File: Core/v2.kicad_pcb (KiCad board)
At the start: 4 copper layers, 80 x 43 mm, 120 parts, among them J1 JST_PH_S4B-PH-K, J2 JST_PH_S4B-PH-K, J3 JST_PH_S3B-PH-K, J4 JST_PH_S6B-PH-K, J5 JST_PH_S6B-PH-K, J6 Conn_02x06_Odd_Even, J7 Conn_01x02_Male, J8 Conn_01x02_Male, J9 Conn_02x06_Odd_Even, Q1 STD2805, U1 ADAU1452, U2 24AA1024, U3 AD1974, U4 AD1955, U5 AD1955, Y1 12.288MHz, Y2 12.288MHz

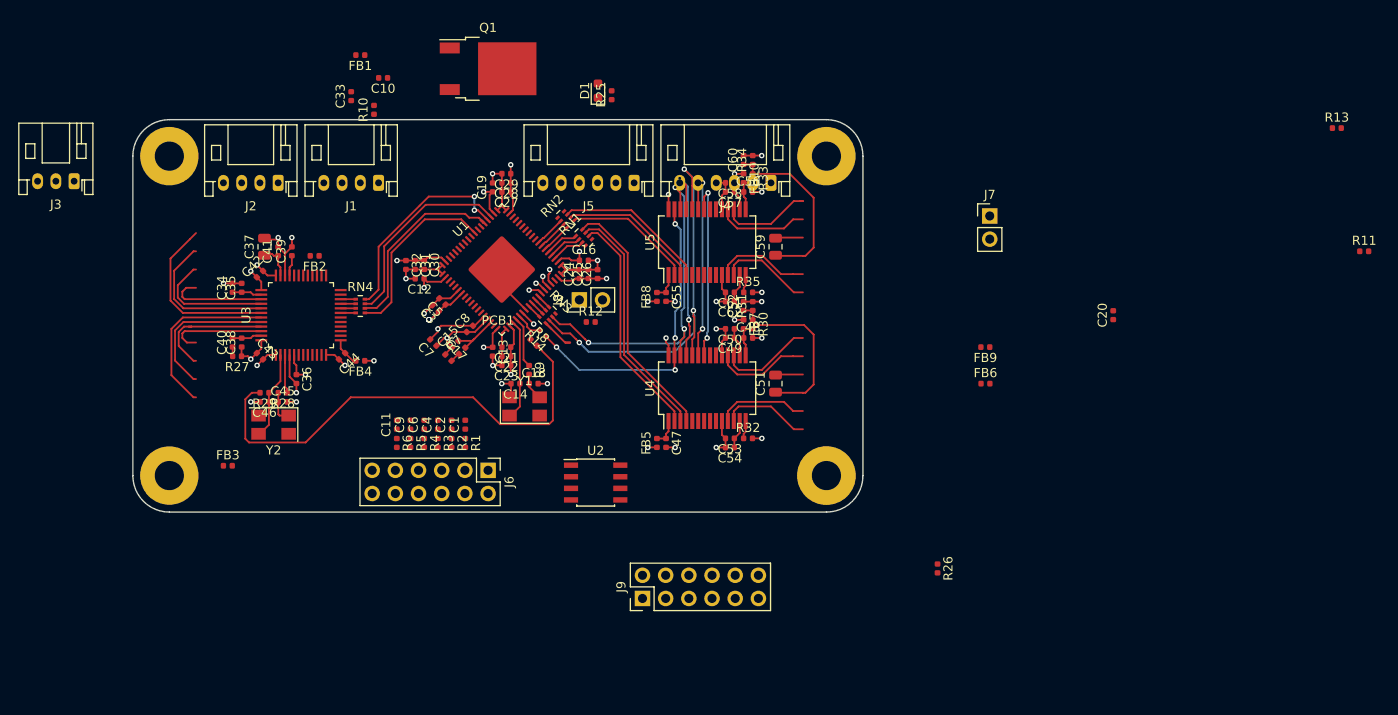
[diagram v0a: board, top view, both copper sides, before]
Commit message: Update partial routing
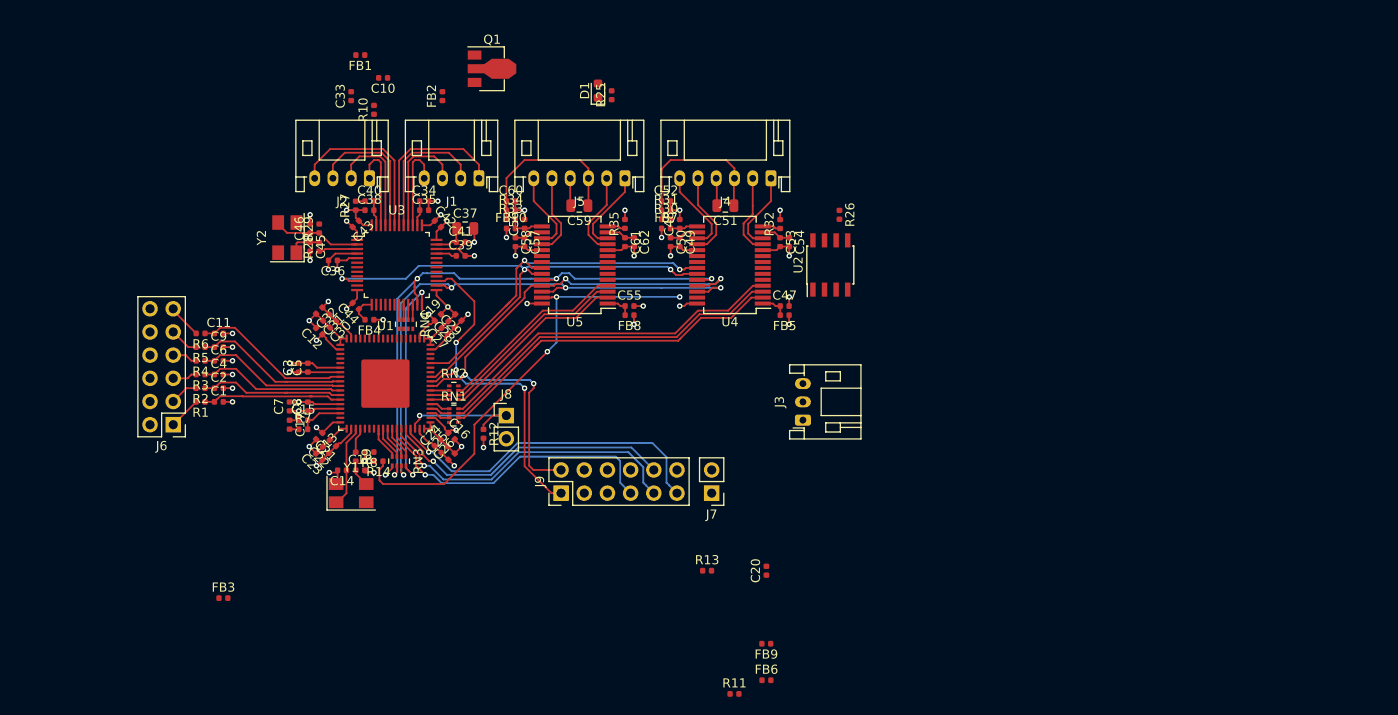
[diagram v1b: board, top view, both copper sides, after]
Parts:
- removed PCB1: Board_Module, PCB:PCB_Board_70x43
- Q1: footprint Package_TO_SOT_SMD:TO-252-2 -> Package_TO_SOT_SMD:SOT-89-3
- moved R11 84.3 mm to (176.5, 140.0)
- moved R13 84.3 mm to (173.5, 126.5)
- moved J3 84.0 mm to (184.0, 110.0), turned to 90 degrees
- moved C20 47.2 mm to (180.0, 126.5)
- moved J7 43.0 mm to (174.0, 118.0), turned to 180 degrees
- moved FB6 40.4 mm to (180.0, 138.5)
- moved FB9 40.4 mm to (180.0, 134.5)
- moved R26 40.2 mm to (188.0, 87.5)
- moved U2 35.1 mm to (187.0, 93.0), turned to 90 degrees
- moved J6 34.9 mm to (115.0, 110.5), turned to 180 degrees
- moved R1 29.3 mm to (118.0, 108.0), turned to 180 degrees
- moved R2 28.1 mm to (118.0, 106.5), turned to 180 degrees
- moved C1 27.1 mm to (120.0, 108.0), turned to 0 degrees
- moved R34 27.1 mm to (152.0, 87.0), turned to 0 degrees
- moved R3 27.1 mm to (118.0, 105.0), turned to 180 degrees
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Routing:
- net /DSP/I2S_MCLK_ADC: track 52.5 -> 1.01 mm, vias 0 -> 1
- net /ADC/SPI_CS: track 0.00 -> 39.3 mm, vias 0 -> 3
- net /DAC1/SPI_CS: track 23.7 -> 62.4 mm, vias 2 -> 4
- net /DSP/ENABLE: track 22.2 -> 60.8 mm, vias 2 -> 3
- net /DSP/SS: track 1.73 -> 36.7 mm
- net /DSP/SCLK: track 1.29 -> 35.0 mm
- net /DSP/MISO: track 1.52 -> 33.5 mm
- net /DSP/MOSI: track 1.39 -> 32.1 mm
- net /ADC/SPI_CLK: track 38.6 -> 64.2 mm, vias 3 -> 4
- net /ADC/SPI_MISO: track 0.00 -> 23.7 mm, vias 0 -> 2
- net /ADC/I2S_LRCLK: track 22.8 -> 0.00 mm, vias 2 -> 0
- net /ADC/I2S_BCLK: track 21.7 -> 0.00 mm
- net /ADC/I2S_SDIN1: track 21.7 -> 0.06 mm
- net /ADC/I2S_SDIN2: track 20.1 -> 0.00 mm
- net /DSP/MUTE: track 20.1 -> 39.0 mm
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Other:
- board outline removed

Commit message: Update partial routing
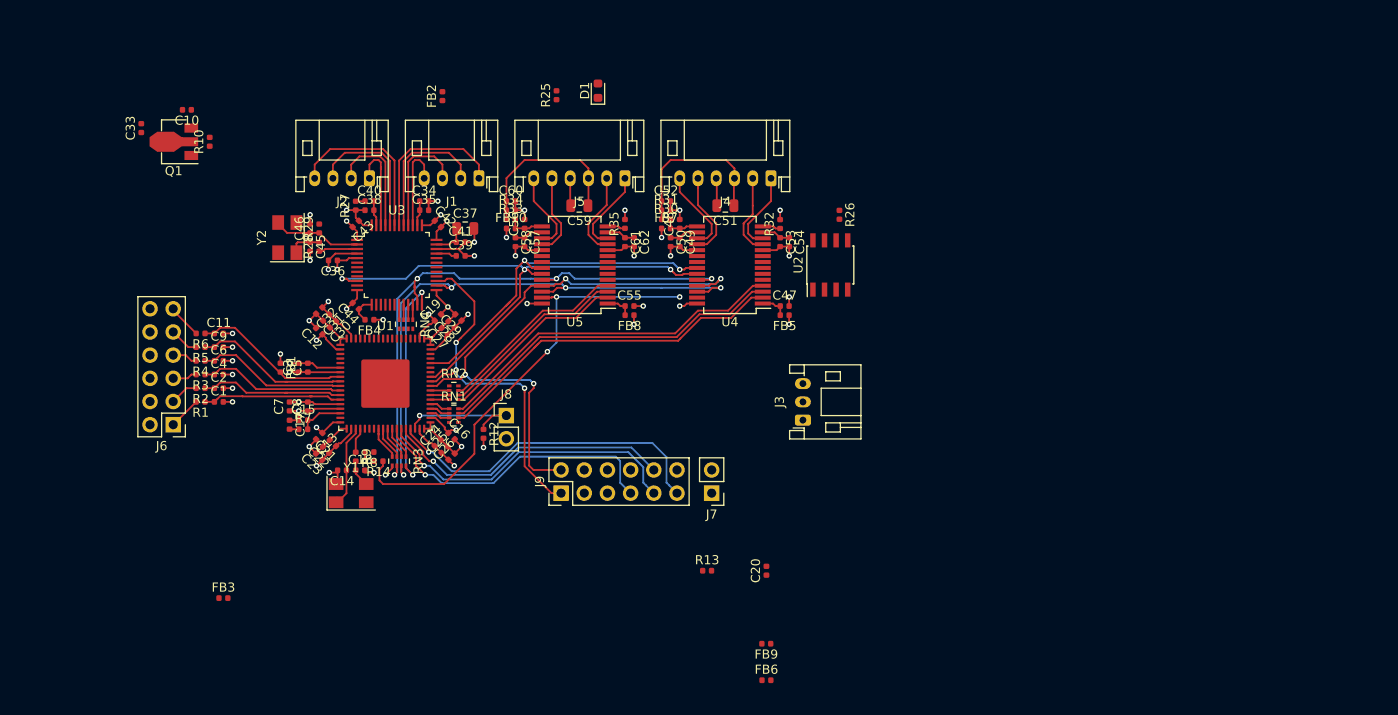
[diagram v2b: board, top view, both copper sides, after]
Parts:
- removed R11: 0R, Resistor_SMD:R_0402_1005Metric
- moved FB1 35.4 mm to (126.8, 104.2), turned to 270 degrees
- moved Q1 34.9 mm to (115.5, 79.5), turned to 180 degrees
- moved C33 23.3 mm to (111.5, 78.0)
- moved C10 21.8 mm to (116.5, 76.0)
- moved R10 18.3 mm to (119.0, 79.5)
- moved R25 6.04 mm to (157.0, 74.4)
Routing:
- net +3V3: track 16.5 -> 17.6 mm, vias 6 -> 7
- added copper zone on In2.Cu, net /DSP/DVDD
- added copper zone on In2.Cu, net Net-(C36-Pad1)
- removed copper zone on In1.Cu, net GNDA

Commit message: Add complete routing
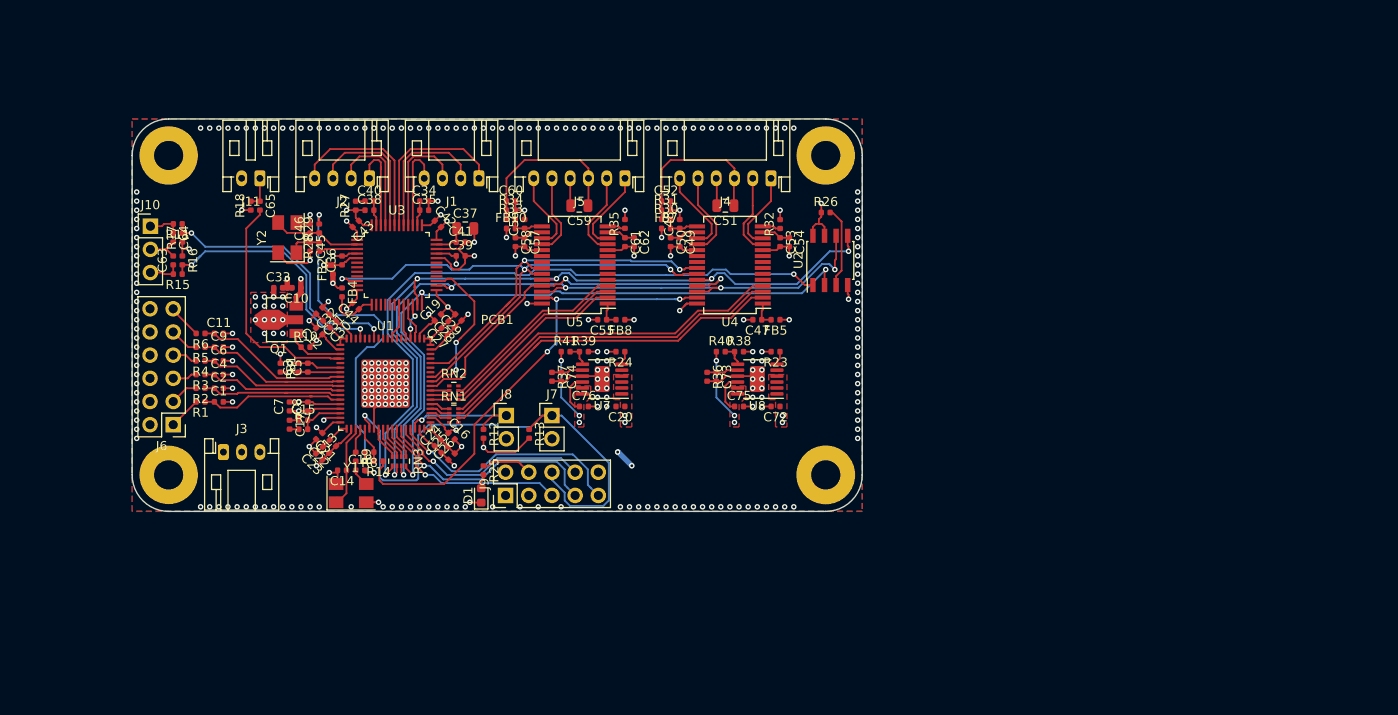
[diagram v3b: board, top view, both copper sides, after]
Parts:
- removed FB3, FB6, FB9: 600Z, Inductor_SMD:L_0402_1005Metric
- removed RN4: 33R, Resistor_SMD:R_Array_Concave_4x0402
- added C63: 10n, Capacitor_SMD:C_0402_1005Metric, F.Cu at (115.0, 92.5)
- added C64: 10n, Capacitor_SMD:C_0402_1005Metric, F.Cu at (115.0, 90.0)
- added C65: 10n, Capacitor_SMD:C_0402_1005Metric, F.Cu at (124.5, 86.5)
- added C72: 10u, Capacitor_SMD:C_0402_1005Metric, F.Cu at (181.0, 108.5)
- added C73: 1u, Capacitor_SMD:C_0402_1005Metric, F.Cu at (174.5, 105.2)
- added C74: 1u, Capacitor_SMD:C_0402_1005Metric, F.Cu at (157.5, 105.2)
- added C75: 10u, Capacitor_SMD:C_0402_1005Metric, F.Cu at (177.0, 108.5)
- added C76: 10u, Capacitor_SMD:C_0402_1005Metric, F.Cu at (160.0, 108.5)
- added J10: Conn_01x03_Male, Connector_PinHeader_2.54mm:PinHeader_1x03_P2.54mm_Vertical, F.Cu at (112.5, 88.8)
- added J11: Conn_01x02_Male, Connector_JST:JST_PH_S2B-PH-K_1x02_P2.00mm_Horizontal, F.Cu at (124.5, 83.5)
- added PCB1: Board_Module, Library:PCB_Board_70x43, F.Cu at (150.5, 98.5)
- added R11: 10k, Resistor_SMD:R_0402_1005Metric, F.Cu at (115.5, 88.5)
- added R15: 10k, Resistor_SMD:R_0402_1005Metric, F.Cu at (115.5, 94.0)
- added R16: 10k, Resistor_SMD:R_0402_1005Metric, F.Cu at (116.0, 92.5)
- added R17: 10k, Resistor_SMD:R_0402_1005Metric, F.Cu at (116.0, 90.0)
- added R18: 10k, Resistor_SMD:R_0402_1005Metric, F.Cu at (123.5, 86.5)
- added R23: 0R, Resistor_SMD:R_0402_1005Metric, F.Cu at (181.0, 102.5)
- added R24: 0R, Resistor_SMD:R_0402_1005Metric, F.Cu at (164.0, 102.5)
- added R36: 5k, Resistor_SMD:R_0402_1005Metric, F.Cu at (173.5, 105.2)
- added R37: 3.3k, Resistor_SMD:R_0402_1005Metric, F.Cu at (156.5, 105.2)
- added R38: 18k, Resistor_SMD:R_0402_1005Metric, F.Cu at (177.0, 102.5)
- added R39: 18k, Resistor_SMD:R_0402_1005Metric, F.Cu at (160.0, 102.5)
- added R40: 750k, Resistor_SMD:R_0402_1005Metric, F.Cu at (175.0, 102.5)
- added R41: 750k, Resistor_SMD:R_0402_1005Metric, F.Cu at (158.0, 102.5)
- added U7: LT3045, Package_SO:MSOP-12-1EP_3x4mm_P0.65mm_EP1.65x2.85mm, F.Cu at (162.0, 105.5)
- added U8: LT3045, Package_SO:MSOP-12-1EP_3x4mm_P0.65mm_EP1.65x2.85mm, F.Cu at (179.0, 105.5)
- C20: value 100n -> 10u
- J9: value Conn_02x06_Odd_Even -> Conn_02x05_Odd_Even; footprint Connector_PinHeader_2.54mm:PinHeader_2x06_P2.54mm_Vertical -> Connector_PinHeader_2.54mm:PinHeader_2x05_P2.54mm_Vertical
- Q1: value STD2805 -> 2STF2550
- moved J3 63.6 mm to (120.5, 113.5), turned to 0 degrees
- moved D1 46.2 mm to (148.8, 118.2)
- moved R25 41.9 mm to (149.0, 115.5), turned to 270 degrees
- moved R10 24.8 mm to (129.5, 102.0), turned to 0 degrees
- moved R13 24.6 mm to (154.0, 111.5), turned to 270 degrees
- moved C20 24.1 mm to (164.0, 108.5), turned to 180 degrees
- moved C33 23.0 mm to (126.5, 95.5), turned to 0 degrees
- moved C10 22.9 mm to (128.5, 95.5)
- moved Q1 22.6 mm to (127.0, 99.0)
- moved FB2 22.5 mm to (132.5, 93.5)
- moved J7 19.5 mm to (156.5, 109.5), turned to 0 degrees
- moved J9 6.09 mm to (151.4, 118.2)
- moved FB4 4.24 mm to (133.5, 96.0), turned to 270 degrees
- moved C47 3.35 mm to (179.0, 99.0), turned to 180 degrees
- moved C55 3.35 mm to (162.0, 99.0), turned to 180 degrees
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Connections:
- C10 pad 1: +3V3 -> VDD
- C12 pad 1: +3V3 -> VDD
- C13 pad 1: +3V3 -> VDD
- C16 pad 1: +3V3 -> VDD
- C19 pad 1: +3V3 -> VDD
- C20 pad 1: +3V3 -> /6V
- C34 pad 2: GNDA -> GND
- C35 pad 2: GNDA -> GND
- C36 pad 2: GNDA -> GND
- C37 pad 2: GNDA -> GND
- C39 pad 2: GNDA -> GND
- C41 pad 2: GNDA -> GND
- C42 pad 2: GNDA -> GND
- C43 pad 2: GNDA -> GND
- C48 pad 2: GNDA -> GND
- C49 pad 2: GNDA -> GND
- C50 pad 2: GNDA -> GND
- C51 pad 2: GNDA -> GND
- C52 pad 2: GNDA -> GND
- C53 pad 2: GNDA -> GND
- C54 pad 2: GNDA -> GND
- C56 pad 2: GNDA -> GND
- C57 pad 2: GNDA -> GND
- C58 pad 2: GNDA -> GND
- C59 pad 2: GNDA -> GND
- C60 pad 2: GNDA -> GND
- C61 pad 2: GNDA -> GND
- C62 pad 2: GNDA -> GND
- FB1 pad 1: +3V3 -> VDD
- J3 pad 1: +5V -> VDD
- J3 pad 3: +3V3 -> /6V
- J4 pad 4: GNDA -> GND
- J5 pad 4: GNDA -> GND
- J9 pad 1: /ADC/SPI_CS -> Net-(J9-Pad1)
- J9 pad 10: /DSP/MOSI -> GND
- J9 pad 2: /DAC1/SPI_CS -> Net-(J9-Pad2)
- J9 pad 3: (no net) -> Net-(J9-Pad3)
- J9 pad 4: (no net) -> Net-(J9-Pad4)
- J9 pad 5: (no net) -> /DSP/MISO
- J9 pad 6: Net-(J9-Pad6) -> /DSP/nRESET
- J9 pad 7: /DSP/MISO -> /DSP/SCLK
- J9 pad 8: /DSP/nRESET -> /DSP/MOSI
- J9 pad 9: /DSP/SCLK -> /DSP/SS
- Q1 pad 2: Net-(Q1-Pad2) -> /DSP/DVDD
- Q1 pad 3: +3V3 -> VDD
- R10 pad 2: +3V3 -> VDD
- R12 pad 2: +3V3 -> VDD
- R13 pad 2: +3V3 -> VDD
- R25 pad 1: Net-(J9-Pad6) -> Net-(J9-Pad4)
- R26 pad 1: +3V3 -> VDD
- R31 pad 2: GNDA -> GND
- R32 pad 2: GNDA -> GND
- R34 pad 2: GNDA -> GND
- R35 pad 2: GNDA -> GND
- RN1 pad 4: (no net) -> Net-(RN1-Pad4)
- RN1 pad 5: (no net) -> Net-(RN1-Pad5)
- RN2 pad 1: (no net) -> Net-(RN2-Pad1)
- RN2 pad 8: (no net) -> Net-(RN2-Pad8)
- U1 pad 18: +3V3 -> VDD
- U1 pad 2: +3V3 -> VDD
- U1 pad 38: +3V3 -> VDD
- U1 pad 4: (no net) -> Net-(C65-Pad2)
- U1 pad 48: (no net) -> Net-(U1-Pad48)
- U1 pad 49: (no net) -> Net-(U1-Pad49)
- U1 pad 5: (no net) -> Net-(U1-Pad5)
- U1 pad 51: (no net) -> Net-(U1-Pad51)
- U1 pad 52: (no net) -> Net-(U1-Pad52)
- U1 pad 56: +3V3 -> VDD
- U1 pad 60: (no net) -> Net-(U1-Pad60)
- U1 pad 61: (no net) -> Net-(U1-Pad61)
- U1 pad 63: (no net) -> Net-(U1-Pad63)
- U1 pad 64: (no net) -> Net-(U1-Pad64)
- U1 pad 65: (no net) -> Net-(U1-Pad65)
- U1 pad 66: (no net) -> /DSP/A-MP12
- U1 pad 67: (no net) -> Net-(U1-Pad67)
- U1 pad 68: (no net) -> Net-(U1-Pad68)
- U1 pad 69: (no net) -> /DSP/B-MP13
- U1 pad 70: (no net) -> Net-(U1-Pad70)
- U2 pad 7: +3V3 -> VDD
- U2 pad 8: +3V3 -> VDD
- U3 pad 1: GNDA -> GND
- U3 pad 14: (no net) -> Net-(U3-Pad14)
- U3 pad 15: (no net) -> Net-(U3-Pad15)
- U3 pad 16: Net-(U3-Pad11) -> Net-(U3-Pad16)
- U3 pad 17: (no net) -> Net-(U3-Pad17)
- U3 pad 18: (no net) -> Net-(U3-Pad18)
- U3 pad 19: Net-(RN4-Pad4) -> /ADC/I2S_SDIN2
- U3 pad 20: Net-(RN4-Pad3) -> /ADC/I2S_SDIN1
- U3 pad 21: Net-(RN4-Pad2) -> /ADC/I2S_BCLK
- U3 pad 22: Net-(RN4-Pad1) -> /ADC/I2S_LRCLK
- U3 pad 28: Net-(U3-Pad11) -> Net-(U3-Pad28)
- U3 pad 29: Net-(U3-Pad11) -> Net-(U3-Pad29)
- U3 pad 30: Net-(U3-Pad11) -> Net-(U3-Pad30)
- U3 pad 31: Net-(U3-Pad11) -> Net-(U3-Pad31)
- U3 pad 32: GNDA -> GND
- U3 pad 34: GNDA -> GND
- U3 pad 36: GNDA -> GND
- U3 pad 4: GNDA -> GND
- U3 pad 6: Net-(U3-Pad11) -> Net-(U3-Pad6)
- U3 pad 7: Net-(U3-Pad11) -> Net-(U3-Pad7)
- U3 pad 8: Net-(U3-Pad11) -> Net-(U3-Pad8)
- U3 pad 9: Net-(U3-Pad11) -> Net-(U3-Pad9)
- U4 pad 10: GNDA -> GND
- U4 pad 19: GNDA -> GND
- U4 pad 20: (no net) -> Net-(U4-Pad20)
- U4 pad 21: (no net) -> Net-(U4-Pad21)
- U4 pad 5: (no net) -> Net-(U4-Pad5)
- U4 pad 6: (no net) -> Net-(U4-Pad6)
- U4 pad 7: (no net) -> Net-(U4-Pad7)
- U4 pad 8: (no net) -> Net-(U4-Pad8)
- U4 pad 9: (no net) -> Net-(U4-Pad9)
- U5 pad 10: GNDA -> GND
- U5 pad 19: GNDA -> GND
- U5 pad 20: (no net) -> Net-(U5-Pad20)
- U5 pad 21: (no net) -> Net-(U5-Pad21)
- U5 pad 5: (no net) -> Net-(U5-Pad5)
- U5 pad 6: (no net) -> Net-(U5-Pad6)
- U5 pad 7: (no net) -> Net-(U5-Pad7)
- U5 pad 8: (no net) -> Net-(U5-Pad8)
- U5 pad 9: (no net) -> Net-(U5-Pad9)
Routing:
- net VDD: track 0.00 -> 230.1 mm, vias 0 -> 12
- net GND: track 63.1 -> 159.8 mm, vias 21 -> 288
- net +5V: track 3.98 -> 84.0 mm, vias 4 -> 7
- net Net-(RN3-Pad5): track 1.31 -> 72.2 mm, vias 1 -> 2
- net /6V: track 0.00 -> 67.7 mm, vias 0 -> 4
- net /DSP/nRESET: track 0.00 -> 58.7 mm, vias 0 -> 1
- net GNDA: track 50.5 -> 0.00 mm, vias 14 -> 0
- net /ADC/SPI_MISO: track 23.7 -> 72.6 mm, vias 2 -> 3
- net +3V3: track 17.6 -> 54.8 mm, vias 7 -> 4
- net /DSP/I2S_MCLK_ADC: track 1.01 -> 36.7 mm, vias 1 -> 2
- net /DSP/A-MP12: track 0.00 -> 29.7 mm, vias 0 -> 2
- net /DSP/B-MP13: track 0.00 -> 28.7 mm, vias 0 -> 2
- net Net-(C65-Pad2): track 0.00 -> 26.3 mm
- net Net-(C36-Pad1): track 13.0 -> 38.6 mm, vias 3 -> 4
- net /ADC/SPI_CS: track 39.3 -> 16.9 mm, vias 3 -> 2
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- added copper zone on F.Cu, net +3V3
- added copper zone on F.Cu, net +5V
- added copper zone on F.Cu, net /6V
- added copper zone on F.Cu, net /DSP/DVDD
- added copper zone on B.Cu, net GND
- added copper zone on F.Cu, net GND
- added copper zone on In2.Cu, net GND
- removed copper zone on In2.Cu, net Net-(C36-Pad1)
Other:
- board outline added: 80 x 43 mm
